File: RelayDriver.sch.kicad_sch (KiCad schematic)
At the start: 4 parts, among them J6 MolexMicrofitPlus, K2 G2RL-2A, Q1 DMN61D8LQ

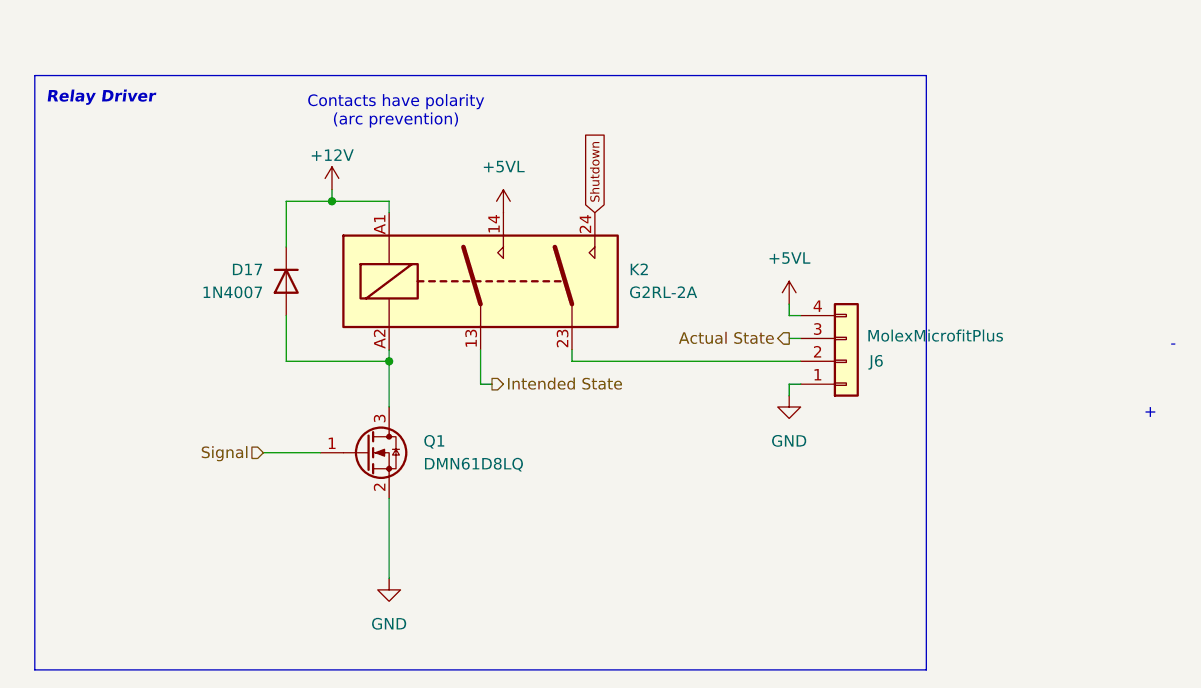
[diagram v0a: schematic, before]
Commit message: Updated to single pole relay, removed relay drivers
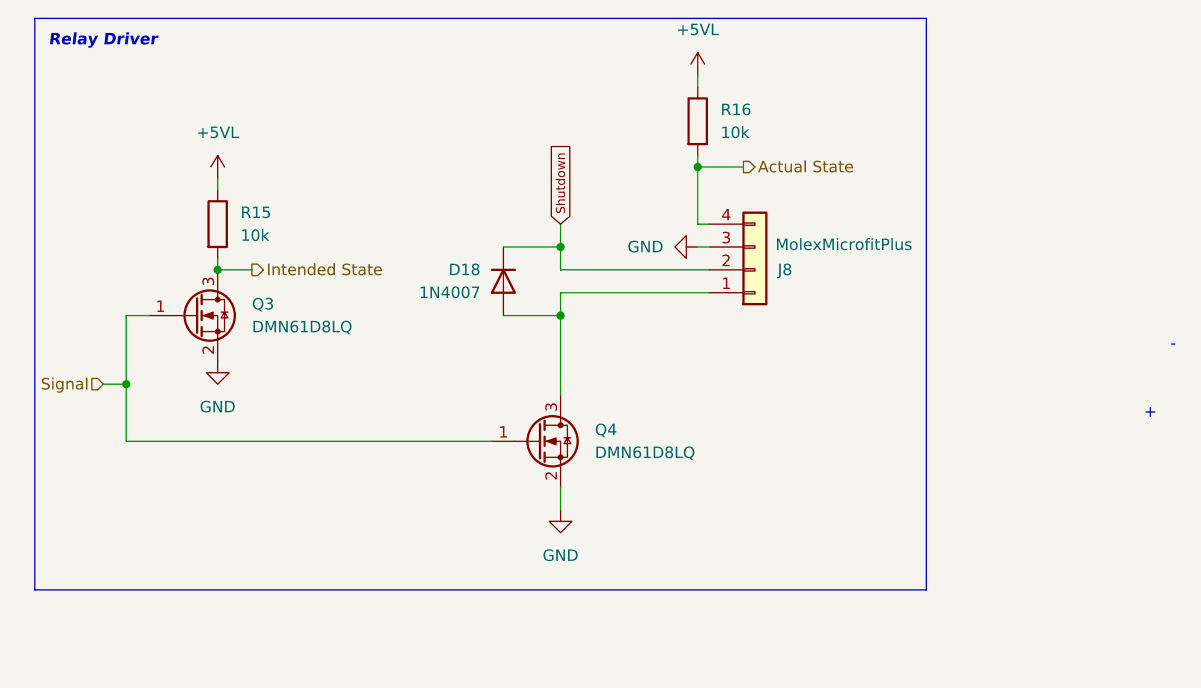
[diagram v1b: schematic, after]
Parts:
- removed K2: G2RL-2A, Relay_THT:Relay_DPST_Omron_G2RL-2A, symbol Relay:G2RL-2A
- added Q3: DMN61D8LQ, Package_TO_SOT_SMD:SOT-23, symbol Transistor_FET:DMN61D8LQ
- added R15, R16: 10k, Resistor_SMD:R_0603_1608Metric, symbol Device:R
- renumbered D17 to D18, J6 to J8, Q1 to Q4
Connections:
- net +12V is gone; now on net Shutdown: D18.1 (K)
- net +5VL: now also R15.1, R16.1; no longer J8.4 (Pin_4)
- net Actual State: now also J8.4 (Pin_4), R16.2; no longer J8.3 (Pin_3)
- net GND: now also J8.3 (Pin_3), Q3.2 (S); no longer J8.1 (Pin_1)
- net Intended State: now also Q3.3 (D), R15.2
- net Shutdown: now also J8.2 (Pin_2)
- net Signal: now also Q3.1 (G)
- net at D18.2 (A), Q4.3 (D): now also J8.1 (Pin_1)
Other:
- note removed: "Contacts have polarity (arc prevention)"
- moved on the sheet: D18, J8, Q4

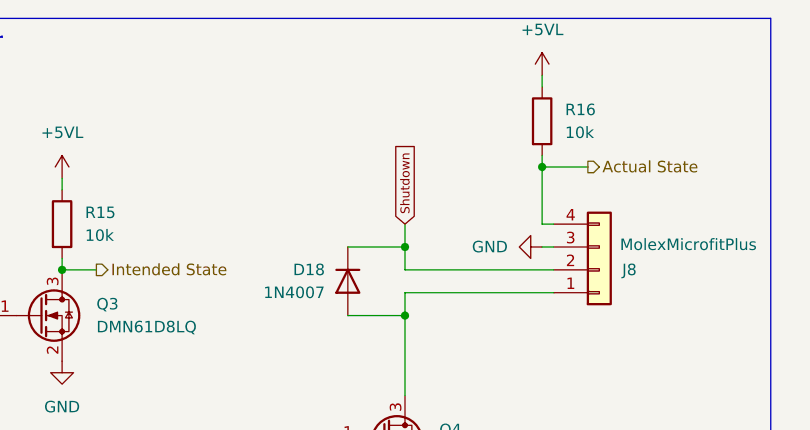
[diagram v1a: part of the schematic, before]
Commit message: schematic: Cleanup all global labels
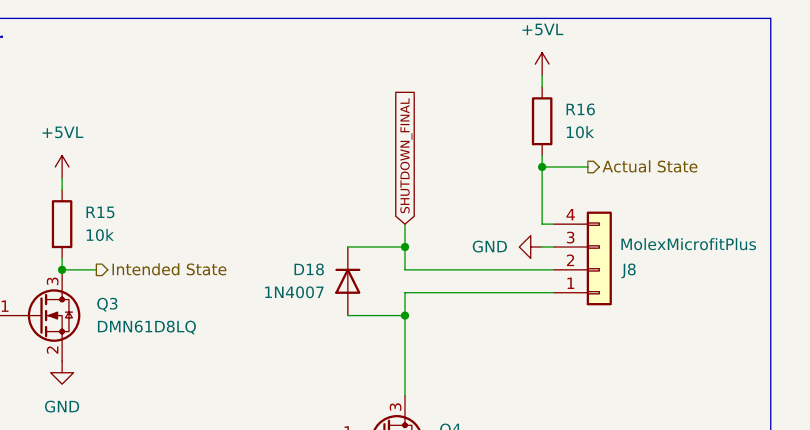
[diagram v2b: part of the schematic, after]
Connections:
- net Shutdown renamed SHUTDOWN_FINAL
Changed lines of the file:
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@@
 		(rev "${REVISION}")
 		(company "York Formula Student")
-		(comment 1 "Designed by Josh B and Logan C")
+		(comment 1 "Designed by Josh B, Logan C, and Owen S")
 	)
 	(rectangle
@@
 		)
 	)
-	(global_label "Shutdown"
+	(global_label "SHUTDOWN_FINAL"
 		(shape input)
 		(at 101.6 73.66 90)
@@
 		)
 		(property "Intersheetrefs" "${INTERSHEET_REFS}"
-			(at 101.6 64.2143 90)
+			(at 101.6 58.4527 90)
 			(effects
 				(font
